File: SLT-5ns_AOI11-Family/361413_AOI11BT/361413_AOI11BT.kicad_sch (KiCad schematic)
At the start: 21 parts, among them T1 T_DB, T2 T_DB

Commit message: Updated schematics
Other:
- note removed: "B"
- note removed: "C"
- note removed: "E"
- note removed: "Transistor Die Layout (top view)"
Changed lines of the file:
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@@
     (stroke (width 0) (type default) (color 0 0 0 0))
-  )
-  (polyline (pts (xy 252.73 29.21) (xy 252.73 40.64))
-    (stroke (width 0) (type solid) (color 0 0 0 0))
   )
   (wire (pts (xy 53.34 72.39) (xy 60.96 72.39))
     (stroke (width 0) (type default) (color 0 0 0 0))
-  )
-  (polyline (pts (xy 264.16 40.64) (xy 252.73 40.64))
-    (stroke (width 0) (type solid) (color 0 0 0 0))
   )
   (wire (pts (xy 120.65 115.57) (xy 147.32 115.57))
@@
   (wire (pts (xy 78.74 58.42) (xy 68.58 58.42))
     (stroke (width 0) (type default) (color 0 0 0 0))
-  )
-  (polyline (pts (xy 252.73 29.21) (xy 264.16 29.21))
-    (stroke (width 0) (type solid) (color 0 0 0 0))
   )
   (wire (pts (xy 132.08 78.74) (xy 120.65 78.74))
@@
   (wire (pts (xy 152.4 143.51) (xy 152.4 139.7))
     (stroke (width 0) (type default) (color 0 0 0 0))
-  )
-  (polyline (pts (xy 264.16 29.21) (xy 264.16 40.64))
-    (stroke (width 0) (type solid) (color 0 0 0 0))
   )
   (wire (pts (xy 139.7 66.04) (xy 152.4 66.04))
@@
     (effects (font (size 1.27 1.27)) (justify left bottom))
   )
-  (text "C" (at 257.81 39.37 0)
-    (effects (font (size 1.27 1.27)) (justify left bottom))
-  )
   (text "AND Extend" (at 59.69 99.06 0)
     (effects (font (size 1.27 1.27)) (justify left bottom))
   )
-  (text "E" (at 254 33.02 0)
-    (effects (font (size 1.27 1.27)) (justify left bottom))
-  )
-  (text "B" (at 261.62 33.02 0)
-    (effects (font (size 1.27 1.27)) (justify left bottom))
-  )
-  (text "Transistor Die Layout (top view)" (at 243.84 27.94 0)
-    (effects (font (size 1.27 1.27)) (justify left bottom))
-  )

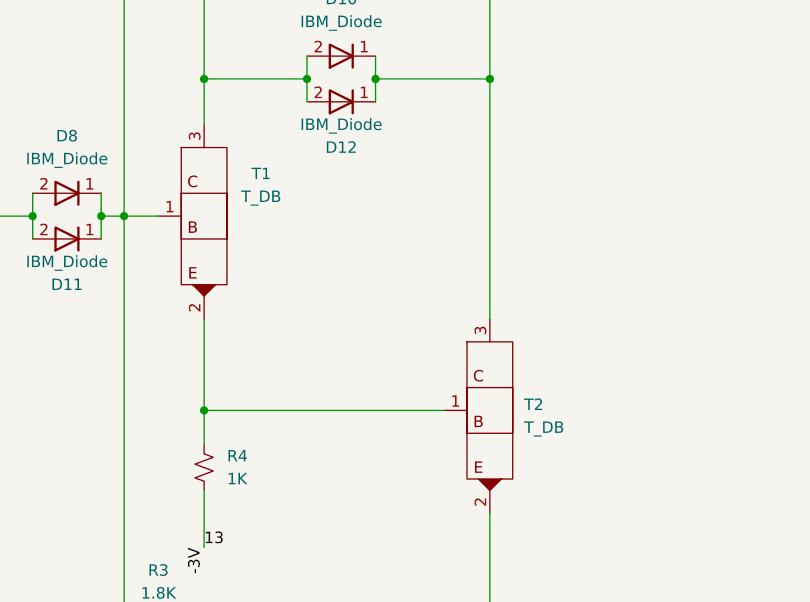
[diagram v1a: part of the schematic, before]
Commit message: Finished off the SLT-30 family of parts, started on the SLT-700 family. Changed labeling of transistors and diodes in all schematics, but have yet to update all the pdf files. This is a TODO...
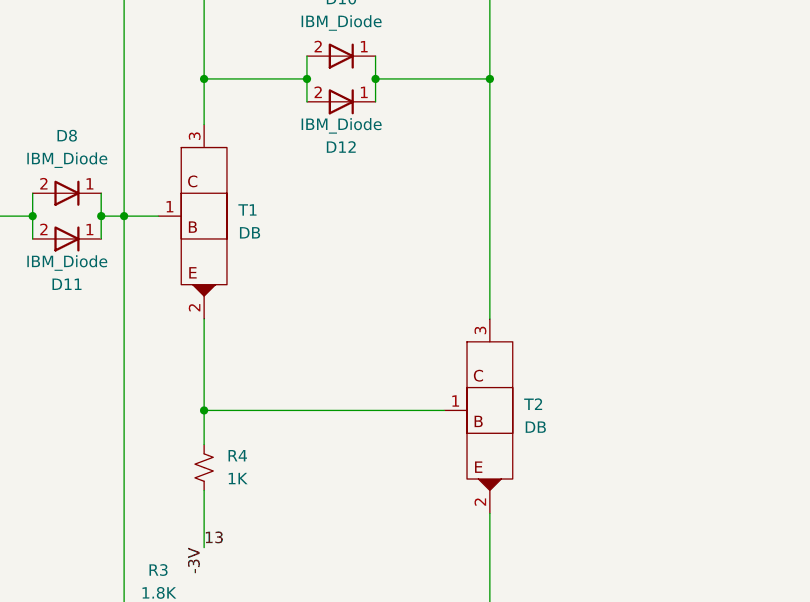
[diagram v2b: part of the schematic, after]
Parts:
- T1, T2: value T_DB -> DB
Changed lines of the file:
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@@
   (symbol (lib_id "IBM_SLT-SLD:T_DB") (at 120.65 93.98 0) (unit 1)
     (in_bom yes) (on_board yes) (fields_autoplaced)
-    (property "Reference" "T1" (id 0) (at 127 89.281 0))
-    (property "Value" "T_DB" (id 1) (at 127 91.821 0))
+    (property "Reference" "T1" (id 0) (at 124.46 93.3449 0)
+      (effects (font (size 1.27 1.27)) (justify left))
+    )
+    (property "Value" "DB" (id 1) (at 124.46 95.8849 0)
+      (effects (font (size 1.27 1.27)) (justify left))
+    )
     (property "Footprint" "Package_DFN_QFN:Diodes_DFN1006-3" (id 2) (at 120.65 93.98 0)
       (effects (font (size 1.27 1.27)) hide)
@@
       (effects (font (size 1.27 1.27)) (justify left))
     )
-    (property "Value" "T_DB" (id 1) (at 156.21 117.4749 0)
+    (property "Value" "DB" (id 1) (at 156.21 117.4749 0)
       (effects (font (size 1.27 1.27)) (justify left))
     )
@@
     )
     (path "/95303cff-6932-4821-b7e1-1e8ef06881c6"
-      (reference "T1") (unit 1) (value "T_DB") (footprint "Package_DFN_QFN:Diodes_DFN1006-3")
+      (reference "T1") (unit 1) (value "DB") (footprint "Package_DFN_QFN:Diodes_DFN1006-3")
     )
     (path "/aca742d5-d20c-41e7-9ac8-8b36b22cfba4"
-      (reference "T2") (unit 1) (value "T_DB") (footprint "Package_DFN_QFN:Diodes_DFN1006-3")
+      (reference "T2") (unit 1) (value "DB") (footprint "Package_DFN_QFN:Diodes_DFN1006-3")
     )
     (path "/98cf94aa-9a14-4efb-965e-894e721f61fd"
